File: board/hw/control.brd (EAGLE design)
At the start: 100 x 80 mm, 38 parts, among them T1 pn2222a, T2 pn2222a, T3 pn2222a, T4 pn2222a, T5 pn2222a, T6 pn2222a, T7 pn2222a, T8 pn2222a

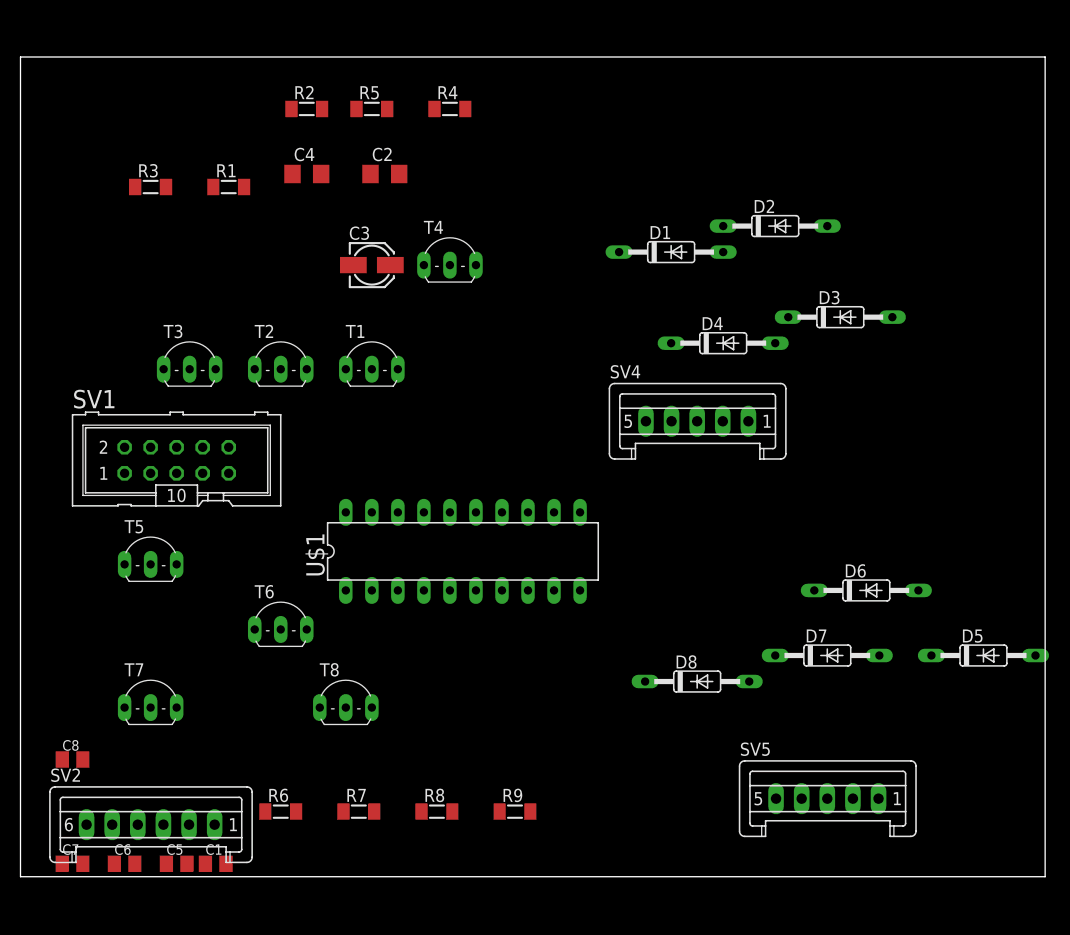
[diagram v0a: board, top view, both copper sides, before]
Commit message: removed capacitors for buttons - these are already covered by the external board
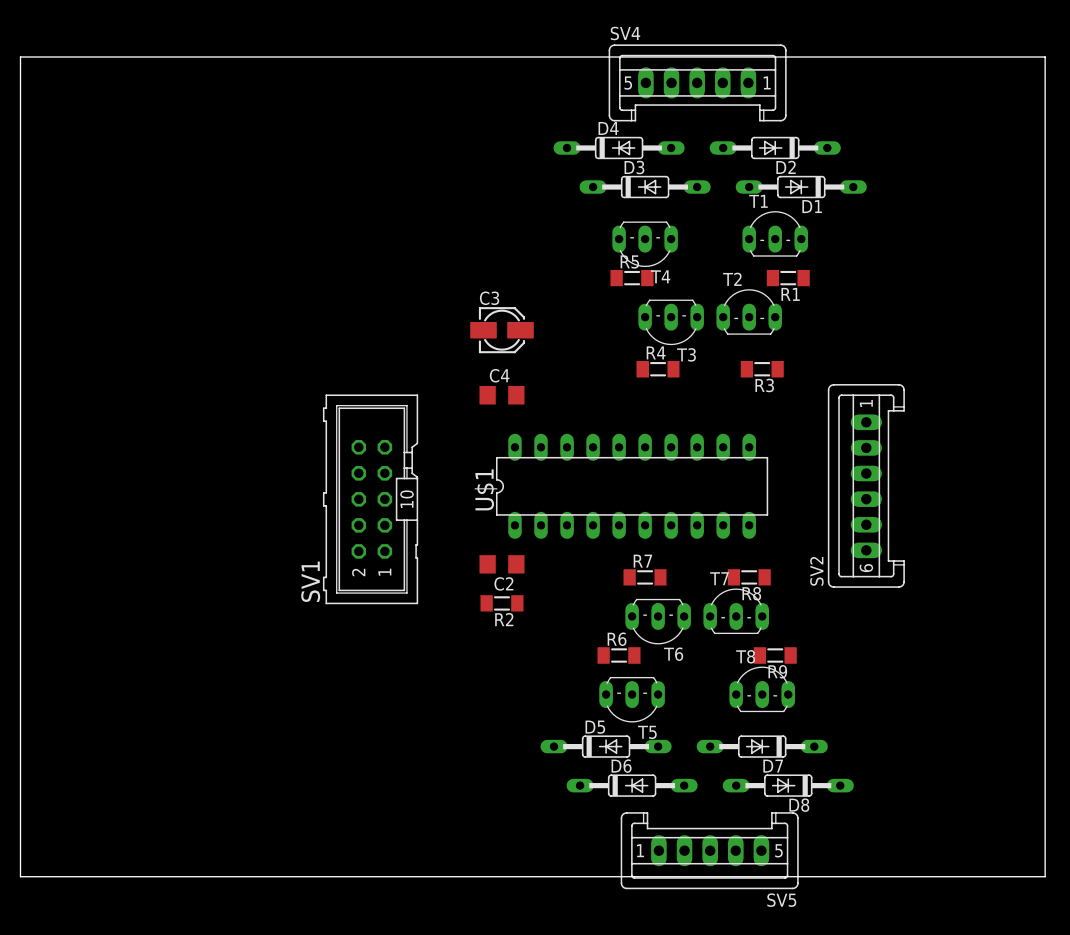
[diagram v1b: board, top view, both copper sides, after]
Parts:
- removed C1, C5, C6, C7, C8: 10nF, rcl:C0805K
- moved SV2 77.3 mm to (82.5, 38.1), turned to 90 degrees
- moved R3 62.3 mm to (72.4, 49.5), turned to 180 degrees
- moved T7 57.8 mm to (69.8, 25.4)
- moved R1 55.3 mm to (74.9, 58.4), turned to 180 degrees
- moved R2 51.9 mm to (47.0, 26.7), turned to 180 degrees
- moved T5 48.7 mm to (59.7, 17.8), turned to 180 degrees
- moved T3 47.3 mm to (63.5, 54.6), turned to 180 degrees
- moved T2 46.0 mm to (71.1, 54.6)
- moved T1 41.4 mm to (73.7, 62.2)
- moved T8 40.7 mm to (72.4, 17.8)
- moved C2 39.8 mm to (47.0, 30.5), turned to 180 degrees
- moved R8 38.1 mm to (71.1, 29.2), turned to 180 degrees
- moved D5 37.9 mm to (57.1, 12.7)
- moved T6 36.9 mm to (62.2, 25.4), turned to 180 degrees
- moved R6 36.4 mm to (58.4, 21.6)
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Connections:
- net 0V: no longer C1.2, C5.2, C6.2, C7.2, C8.2
- net N$22: no longer C8.1
- net N$23: no longer C7.1
- net N$24: no longer C6.1
- net N$25: no longer C1.1
- net N$3: no longer C5.1

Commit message: single-layer routing completed (yay)
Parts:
- added D9: 1N4446, diode:DO35-10
- moved SV1 3.59 mm to (36.8, 39.4)
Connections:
- new net N$26: C3.+, C4.2, D9.C, U$1.20
- net +5V: now also D9.A; no longer C3.+, C4.2, U$1.20
- net N$11: now also U$1.13; no longer U$1.14
- net N$13: now also U$1.14; no longer U$1.13
- net N$15: now also U$1.15; no longer U$1.12
- net N$18: now also U$1.6; no longer U$1.7
- net N$6: now also U$1.7; no longer U$1.6
- net N$9: now also U$1.12; no longer U$1.15
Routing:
- net +5V: track 0.00 -> 177.7 mm
- net N$25: track 0.00 -> 41.5 mm
- net N$16: track 0.00 -> 28.7 mm
- net N$24: track 0.00 -> 25.9 mm
- net N$20: track 0.00 -> 23.5 mm
- net N$18: track 0.00 -> 23.0 mm
- net N$21: track 0.00 -> 22.9 mm
- net N$10: track 0.00 -> 22.9 mm
- net N$5: track 0.00 -> 22.9 mm
- net N$12: track 0.00 -> 22.9 mm
- net N$2: track 0.00 -> 22.6 mm
- net N$9: track 0.00 -> 22.4 mm
- net N$17: track 0.00 -> 22.4 mm
- net N$15: track 0.00 -> 21.4 mm
- net N$23: track 0.00 -> 20.1 mm
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- added copper zone on layer 1, net 0V
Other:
- board size 100 x 80 mm -> 56.8 x 82.5 mm

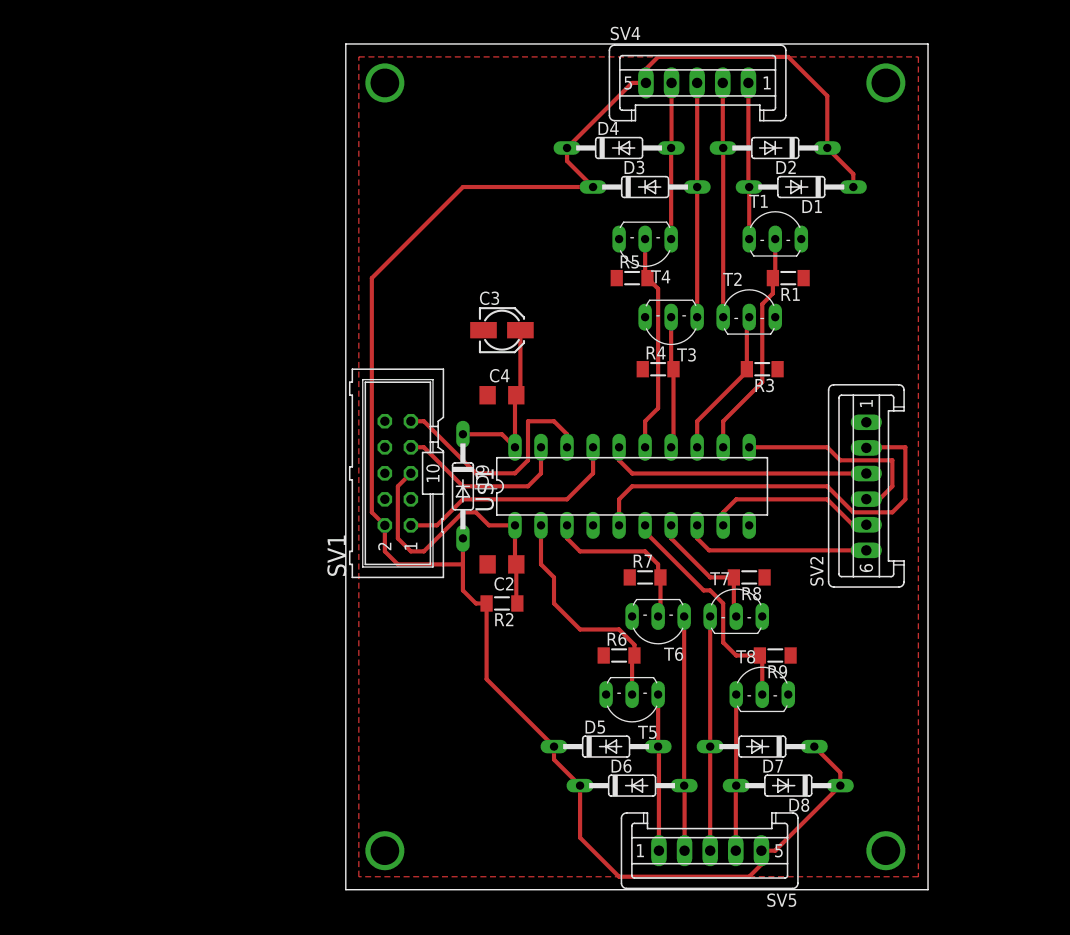
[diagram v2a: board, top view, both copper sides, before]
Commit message: moved KANDA connector in order to simplifiy and reduce board a bit
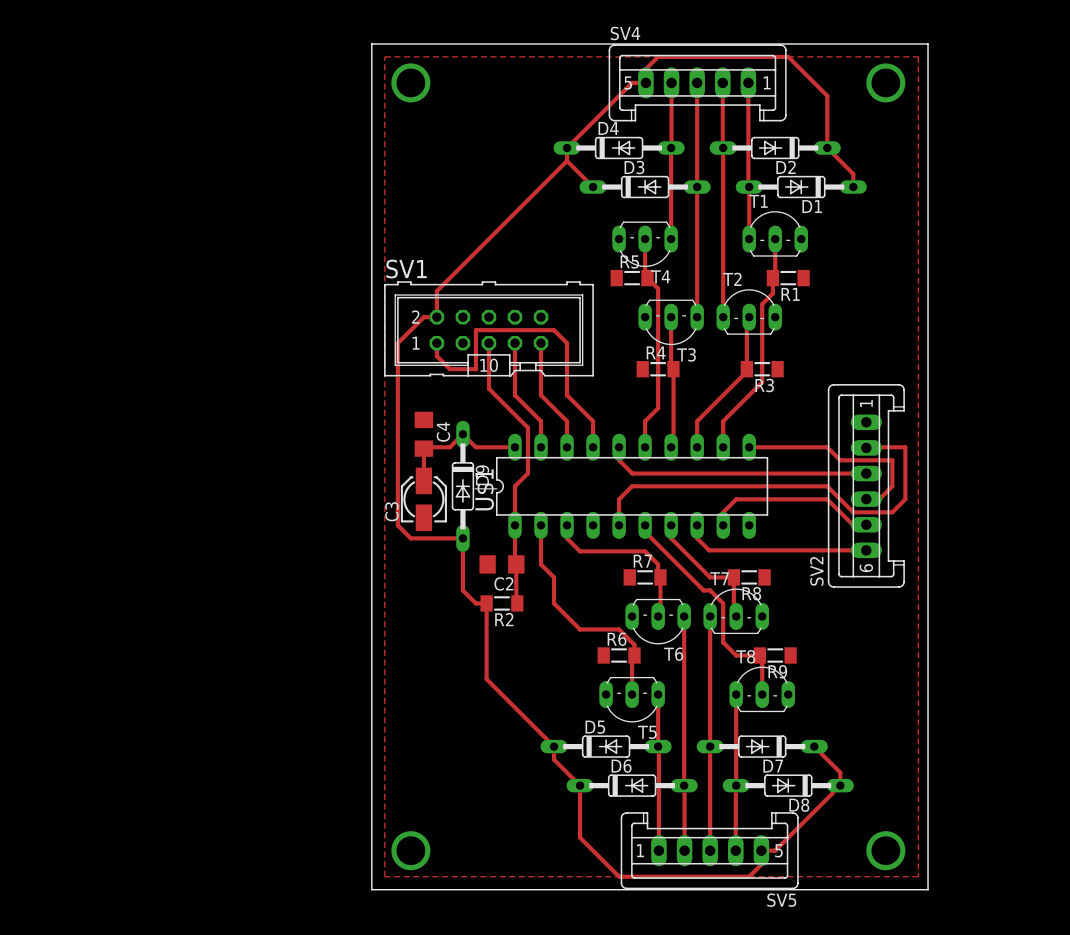
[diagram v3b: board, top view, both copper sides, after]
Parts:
- moved C3 18.2 mm to (39.4, 36.8), turned to 90 degrees
- moved SV1 16.6 mm to (45.7, 53.3), turned to 0 degrees
- moved C4 8.52 mm to (39.4, 43.2), turned to 270 degrees
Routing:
- net N$20: track 23.5 -> 11.2 mm
- net +5V: track 177.7 -> 167.1 mm
- net N$17: track 22.4 -> 30.0 mm
- net N$19: track 17.3 -> 11.2 mm
- net N$26: track 17.3 -> 13.1 mm
- net N$16: track 28.7 -> 27.6 mm
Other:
- board size 56.8 x 82.5 mm -> 54.3 x 82.5 mm
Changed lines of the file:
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@@
 <board>
 <plain>
-<wire x1="31.75" y1="-1.27" x2="88.57" y2="-1.27" width="0" layer="20"/>
+<wire x1="34.29" y1="-1.27" x2="88.57" y2="-1.27" width="0" layer="20"/>
 <wire x1="88.57" y1="-1.27" x2="88.57" y2="81.27" width="0" layer="20"/>
-<wire x1="88.57" y1="81.27" x2="31.75" y2="81.27" width="0" layer="20"/>
-<wire x1="31.75" y1="81.27" x2="31.75" y2="-1.27" width="0" layer="20"/>
+<wire x1="88.57" y1="81.27" x2="34.29" y2="81.27" width="0" layer="20"/>
+<wire x1="34.29" y1="81.27" x2="34.29" y2="-1.27" width="0" layer="20"/>
 </plain>
 <attributes>
@@
 <elements>
 <element name="C2" library="rcl" package="C3216" value="100nF" x="46.99" y="30.48" rot="R180"/>
-<element name="C3" library="rcl" package="153CLV-0405" value="4.7uF" x="46.99" y="53.34"/>
-<element name="C4" library="rcl" package="C3216" value="100nF" x="46.99" y="46.99"/>
+<element name="C3" library="rcl" package="153CLV-0405" value="4.7uF" x="39.37" y="36.83" rot="R90"/>
+<element name="C4" library="rcl" package="C3216" value="100nF" x="39.37" y="43.18" rot="R270"/>
 <element name="R1" library="rcl" package="MINI_MELF-0204W" value="100kR" x="74.93" y="58.42" rot="R180"/>
 <element name="R2" library="rcl" package="MINI_MELF-0204W" value="10kR" x="46.99" y="26.67" rot="R180"/>
@@
 <element name="R4" library="rcl" package="MINI_MELF-0204W" value="100kR" x="62.23" y="49.53"/>
 <element name="R5" library="rcl" package="MINI_MELF-0204W" value="100kR" x="59.69" y="58.42"/>
-<element name="SV1" library="con-harting-ml" package="ML10" value="KANDA" x="36.83" y="39.37" rot="R90"/>
+<element name="SV1" library="con-harting-ml" package="ML10" value="KANDA" x="45.72" y="53.34"/>
 <element name="T1" library="transistor" package="TO92-CBE" value="pn2222a" x="73.66" y="62.23"/>
 <element name="T2" library="transistor" package="TO92-CBE" value="pn2222a" x="71.12" y="54.61"/>
@@
 <contactref element="D1" pad="C"/>
 <contactref element="D9" pad="A"/>
-<wire x1="43.18" y1="33.02" x2="43.18" y2="30.48" width="0.4064" layer="1"/>
-<wire x1="43.18" y1="30.48" x2="43.18" y2="27.94" width="0.4064" layer="1"/>
+<wire x1="43.18" y1="33.02" x2="43.18" y2="27.94" width="0.4064" layer="1"/>
 <wire x1="43.18" y1="27.94" x2="44.45" y2="26.67" width="0.4064" layer="1"/>
 <wire x1="44.45" y1="26.67" x2="45.49" y2="26.67" width="0.4064" layer="1"/>
-<wire x1="35.56" y1="34.29" x2="35.56" y2="31.75" width="0.4064" layer="1"/>
-<wire x1="35.56" y1="31.75" x2="36.83" y2="30.48" width="0.4064" layer="1"/>
-<wire x1="36.83" y1="30.48" x2="43.18" y2="30.48" width="0.4064" layer="1"/>
 <wire x1="72.31" y1="2.54" x2="73.66" y2="2.54" width="0.4064" layer="1"/>
 <wire x1="73.66" y1="2.54" x2="80.01" y2="8.89" width="0.4064" layer="1"/>
@@
 <wire x1="53.34" y1="71.12" x2="53.34" y2="69.85" width="0.4064" layer="1"/>
 <wire x1="53.34" y1="69.85" x2="55.88" y2="67.31" width="0.4064" layer="1"/>
-<wire x1="55.88" y1="67.31" x2="43.18" y2="67.31" width="0.4064" layer="1"/>
-<wire x1="43.18" y1="67.31" x2="34.29" y2="58.42" width="0.4064" layer="1"/>
-<wire x1="34.29" y1="58.42" x2="34.29" y2="35.56" width="0.4064" layer="1"/>
-<wire x1="34.29" y1="35.56" x2="35.56" y2="34.29" width="0.4064" layer="1"/>
 <wire x1="81.28" y1="67.31" x2="81.28" y2="68.58" width="0.4064" layer="1"/>
 <wire x1="81.28" y1="68.58" x2="78.74" y2="71.12" width="0.4064" layer="1"/>
@@
 <wire x1="58.42" y1="0" x2="54.61" y2="3.81" width="0.4064" layer="1"/>
 <wire x1="54.61" y1="3.81" x2="54.61" y2="8.89" width="0.4064" layer="1"/>
+<wire x1="43.18" y1="33.02" x2="38.1" y2="33.02" width="0.4064" layer="1"/>
+<wire x1="38.1" y1="33.02" x2="36.83" y2="34.29" width="0.4064" layer="1"/>
+<wire x1="36.83" y1="34.29" x2="36.83" y2="52.07" width="0.4064" layer="1"/>
+<wire x1="36.83" y1="52.07" x2="39.37" y2="54.61" width="0.4064" layer="1"/>
+<wire x1="39.37" y1="54.61" x2="40.64" y2="54.61" width="0.4064" layer="1"/>
+<wire x1="40.64" y1="54.61" x2="40.64" y2="57.15" width="0.4064" layer="1"/>
+<wire x1="40.64" y1="57.15" x2="53.34" y2="69.85" width="0.4064" layer="1"/>
 </signal>
 <signal name="0V">
@@
 <vertex x="87.63" y="80.01"/>
 <vertex x="87.63" y="0"/>
-<vertex x="33.02" y="0"/>
-<vertex x="33.02" y="80.01"/>
+<vertex x="35.56" y="0"/>
+<vertex x="35.56" y="80.01"/>
 </polygon>
 </signal>
@@
 <wire x1="48.39" y1="30.48" x2="48.39" y2="26.77" width="0.4064" layer="1"/>
 <wire x1="48.39" y1="26.77" x2="48.49" y2="26.67" width="0.4064" layer="1"/>
-<wire x1="38.1" y1="39.37" x2="36.83" y2="38.1" width="0.4064" layer="1"/>
-<wire x1="36.83" y1="38.1" x2="36.83" y2="33.02" width="0.4064" layer="1"/>
-<wire x1="36.83" y1="33.02" x2="38.1" y2="31.75" width="0.4064" layer="1"/>
-<wire x1="38.1" y1="31.75" x2="39.37" y2="31.75" width="0.4064" layer="1"/>
-<wire x1="39.37" y1="31.75" x2="43.18" y2="35.56" width="0.4064" layer="1"/>
-<wire x1="43.18" y1="35.56" x2="44.45" y2="35.56" width="0.4064" layer="1"/>
-<wire x1="44.45" y1="35.56" x2="45.72" y2="34.29" width="0.4064" layer="1"/>
-<wire x1="45.72" y1="34.29" x2="48.26" y2="34.29" width="0.4064" layer="1"/>
+<wire x1="48.26" y1="34.29" x2="48.26" y2="38.1" width="0.4064" layer="1"/>
+<wire x1="48.26" y1="38.1" x2="49.53" y2="39.37" width="0.4064" layer="1"/>
+<wire x1="49.53" y1="39.37" x2="49.53" y2="43.815" width="0.4064" layer="1"/>
+<wire x1="49.53" y1="43.815" x2="45.72" y2="47.625" width="0.4064" layer="1"/>
+<wire x1="45.72" y1="47.625" x2="45.72" y2="52.07" width="0.4064" layer="1"/>
 </signal>
 <signal name="N$17">
 <contactref element="SV1" pad="1"/>
 <contactref element="U$1" pad="17"/>
-<wire x1="38.1" y1="34.29" x2="40.64" y2="34.29" width="0.4064" layer="1"/>
-<wire x1="40.64" y1="34.29" x2="43.18" y2="36.83" width="0.4064" layer="1"/>
-<wire x1="43.18" y1="36.83" x2="53.34" y2="36.83" width="0.4064" layer="1"/>
-<wire x1="53.34" y1="36.83" x2="55.88" y2="39.37" width="0.4064" layer="1"/>
-<wire x1="55.88" y1="39.37" x2="55.88" y2="41.91" width="0.4064" layer="1"/>
+<wire x1="55.88" y1="41.91" x2="55.88" y2="44.45" width="0.4064" layer="1"/>
+<wire x1="55.88" y1="44.45" x2="53.34" y2="46.99" width="0.4064" layer="1"/>
+<wire x1="53.34" y1="46.99" x2="53.34" y2="52.07" width="0.4064" layer="1"/>
+<wire x1="53.34" y1="52.07" x2="52.07" y2="53.34" width="0.4064" layer="1"/>
+<wire x1="52.07" y1="53.34" x2="44.45" y2="53.34" width="0.4064" layer="1"/>
+<wire x1="44.45" y1="53.34" x2="44.45" y2="49.53" width="0.4064" layer="1"/>
+<wire x1="44.45" y1="49.53" x2="41.91" y2="49.53" width="0.4064" layer="1"/>
+<wire x1="41.91" y1="49.53" x2="40.64" y2="50.8" width="0.4064" layer="1"/>
+<wire x1="40.64" y1="50.8" x2="40.64" y2="52.07" width="0.4064" layer="1"/>
 </signal>
 <signal name="N$19">
 <contactref element="SV1" pad="7"/>
 <contactref element="U$1" pad="19"/>
-<wire x1="49.53" y1="38.1" x2="50.8" y2="39.37" width="0.4064" layer="1"/>
-<wire x1="50.8" y1="39.37" x2="50.8" y2="41.91" width="0.4064" layer="1"/>
-<wire x1="38.1" y1="41.91" x2="39.37" y2="41.91" width="0.4064" layer="1"/>
-<wire x1="39.37" y1="41.91" x2="43.18" y2="38.1" width="0.4064" layer="1"/>
-<wire x1="43.18" y1="38.1" x2="49.53" y2="38.1" width="0.4064" layer="1"/>
+<wire x1="50.8" y1="41.91" x2="50.8" y2="44.45" width="0.4064" layer="1"/>
+<wire x1="50.8" y1="44.45" x2="48.26" y2="46.99" width="0.4064" layer="1"/>
+<wire x1="48.26" y1="46.99" x2="48.26" y2="52.07" width="0.4064" layer="1"/>
 </signal>
 <signal name="N$20">
 <contactref element="SV1" pad="9"/>
 <contactref element="U$1" pad="18"/>
-<wire x1="53.34" y1="41.91" x2="53.34" y2="43.18" width="0.4064" layer="1"/>
-<wire x1="53.34" y1="43.18" x2="52.07" y2="44.45" width="0.4064" layer="1"/>
-<wire x1="52.07" y1="44.45" x2="49.53" y2="44.45" width="0.4064" layer="1"/>
-<wire x1="49.53" y1="44.45" x2="49.53" y2="40.64" width="0.4064" layer="1"/>
-<wire x1="49.53" y1="40.64" x2="48.26" y2="39.37" width="0.4064" layer="1"/>
-<wire x1="48.26" y1="39.37" x2="44.45" y2="39.37" width="0.4064" layer="1"/>
-<wire x1="44.45" y1="39.37" x2="39.37" y2="44.45" width="0.4064" layer="1"/>
-<wire x1="39.37" y1="44.45" x2="38.1" y2="44.45" width="0.4064" layer="1"/>
+<wire x1="50.8" y1="52.07" x2="50.8" y2="46.99" width="0.4064" layer="1"/>
+<wire x1="50.8" y1="46.99" x2="53.34" y2="44.45" width="0.4064" layer="1"/>
+<wire x1="53.34" y1="44.45" x2="53.34" y2="41.91" width="0.4064" layer="1"/>
 </signal>
 <signal name="N$1">
@@
 <contactref element="U$1" pad="20"/>
 <contactref element="C4" pad="2"/>
-<wire x1="48.26" y1="41.91" x2="48.26" y2="46.86" width="0.4064" layer="1"/>
-<wire x1="48.26" y1="46.86" x2="48.39" y2="46.99" width="0.4064" layer="1"/>
 <contactref element="C3" pad="+"/>
 <contactref element="D9" pad="C"/>
-<wire x1="43.18" y1="43.18" x2="46.99" y2="43.18" width="0.4064" layer="1"/>
-<wire x1="46.99" y1="43.18" x2="48.26" y2="41.91" width="0.4064" layer="1"/>
-<wire x1="48.79" y1="53.34" x2="48.79" y2="47.39" width="0.4064" layer="1"/>
-<wire x1="48.79" y1="47.39" x2="48.39" y2="46.99" width="0.4064" layer="1"/>
+<wire x1="48.26" y1="41.91" x2="44.45" y2="41.91" width="0.4064" layer="1"/>
+<wire x1="44.45" y1="41.91" x2="43.18" y2="43.18" width="0.4064" layer="1"/>
+<wire x1="43.18" y1="43.18" x2="41.91" y2="41.91" width="0.4064" layer="1"/>
+<wire x1="41.91" y1="41.91" x2="39.5" y2="41.91" width="0.4064" layer="1"/>
+<wire x1="39.5" y1="41.91" x2="39.37" y2="41.78" width="0.4064" layer="1"/>
+<wire x1="39.37" y1="41.78" x2="39.37" y2="38.63" width="0.4064" layer="1"/>
 </signal>
 <signal name="N$27">
-<via x="35.56" y="2.54" extent="1-16" drill="2.8" diameter="2.54"/>
+<via x="38.1" y="2.54" extent="1-16" drill="2.8" diameter="2.54"/>
 </signal>
 <signal name="N$28">
@@
 </signal>
 <signal name="N$30">
-<via x="35.56" y="77.47" extent="1-16" drill="2.8" diameter="2.54"/>
+<via x="38.1" y="77.47" extent="1-16" drill="2.8" diameter="2.54"/>
 </signal>
 </signals>
